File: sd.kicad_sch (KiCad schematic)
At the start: 10 parts, among them J5 Micro_SD_Card_Det1

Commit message: assigned footprint and created PCB file
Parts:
- C28: footprint (none) -> Capacitor_SMD:C_0805_2012Metric
- C29: footprint (none) -> Capacitor_SMD:C_0603_1608Metric
- J5: footprint (none) -> Connector_Card:microSD_HC_Hirose_DM3AT-SF-PEJM5
- R12, R13, R14, R15, R16, R17, R18: footprint (none) -> Resistor_SMD:R_0603_1608Metric
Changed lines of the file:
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@@
 			)
 		)
-		(property "Footprint" ""
+		(property "Footprint" "Resistor_SMD:R_0603_1608Metric"
 			(at 137.922 77.47 90)
 			(hide yes)
@@
 			)
 		)
-		(property "Footprint" ""
+		(property "Footprint" "Connector_Card:microSD_HC_Hirose_DM3AT-SF-PEJM5"
 			(at 64.77 114.3 0)
 			(hide yes)
@@
 			)
 		)
-		(property "Footprint" ""
+		(property "Footprint" "Resistor_SMD:R_0603_1608Metric"
 			(at 150.622 113.03 90)
 			(hide yes)
@@
 			)
 		)
-		(property "Footprint" ""
+		(property "Footprint" "Resistor_SMD:R_0603_1608Metric"
 			(at 173.482 113.03 90)
 			(hide yes)
@@
 			)
 		)
-		(property "Footprint" ""
+		(property "Footprint" "Resistor_SMD:R_0603_1608Metric"
 			(at 148.59 98.298 90)
 			(hide yes)
@@
 			)
 		)
-		(property "Footprint" ""
+		(property "Footprint" "Capacitor_SMD:C_0603_1608Metric"
 			(at 181.3052 100.33 0)
 			(hide yes)
@@
 			)
 		)
-		(property "Footprint" ""
+		(property "Footprint" "Resistor_SMD:R_0603_1608Metric"
 			(at 165.862 77.47 90)
 			(hide yes)
@@
 			)
 		)
-		(property "Footprint" ""
+		(property "Footprint" "Resistor_SMD:R_0603_1608Metric"
 			(at 154.432 77.47 90)
 			(hide yes)
@@
 			)
 		)
-		(property "Footprint" ""
+		(property "Footprint" "Resistor_SMD:R_0603_1608Metric"
 			(at 162.052 113.03 90)
 			(hide yes)
@@
 			)
 		)
-		(property "Footprint" ""
+		(property "Footprint" "Capacitor_SMD:C_0805_2012Metric"
 			(at 169.8752 100.33 0)
 			(hide yes)

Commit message: Updated with new power rails, added sensors and gps symbol
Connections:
- net +3.3V renamed +3.3V_HP
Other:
- note added: "PCB: For high speed layout, keep data lines, CMD and CLK length matched"
- note removed: "PCB: For high speed layout, keep data lines, CMD and CK length matched"
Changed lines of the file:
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@@
 		)
 	)
-	(text "PCB: For high speed layout, keep data lines, CMD and CK length matched"
+	(text "PCB: For high speed layout, keep data lines, CMD and CLK length matched"
 		(exclude_from_sim no)
-		(at 120.65 131.572 0)
+		(at 120.904 131.572 0)
 		(effects
 			(font
@@
 			)
 		)
-		(property "Value" "+3.3V"
+		(property "Value" "+3.3V_HP"
 			(at 194.31 100.3299 90)
 			(show_name no)
@@
 		(in_pos_files yes)
 		(dnp no)
-		(fields_autoplaced yes)
 		(property "Reference" "#PWR063"
 			(at 147.32 119.38 0)
@@
 			)
 		)
-		(property "Value" "+3.3V"
-			(at 139.7 119.3799 90)
-			(show_name no)
-			(do_not_autoplace no)
-			(effects
-				(font
-					(size 1.27 1.27)
-				)
-				(justify left)
+		(property "Value" "+3.3V_HP"
+			(at 135.382 119.38 90)
+			(show_name no)
+			(do_not_autoplace no)
+			(effects
+				(font
+					(size 1.27 1.27)
+				)
 			)
 		)
@@
 		(in_pos_files yes)
 		(dnp no)
-		(fields_autoplaced yes)
 		(property "Reference" "#PWR062"
 			(at 139.7 73.66 0)
@@
 			)
 		)
-		(property "Value" "+3.3V"
-			(at 139.7 64.77 0)
-			(show_name no)
-			(do_not_autoplace no)
-			(effects
-				(font
-					(size 1.27 1.27)
-				)
-			)
-		)
+		(property "Value" "+3.3V_HP"
+			(at 135.382 65.532 0)
+			(show_name no)
+			(do_not_autoplace no)
+			(effects
+				(font
+					(size 1.27 1.27)
+				)
+				(justify left)
+			)
+		)

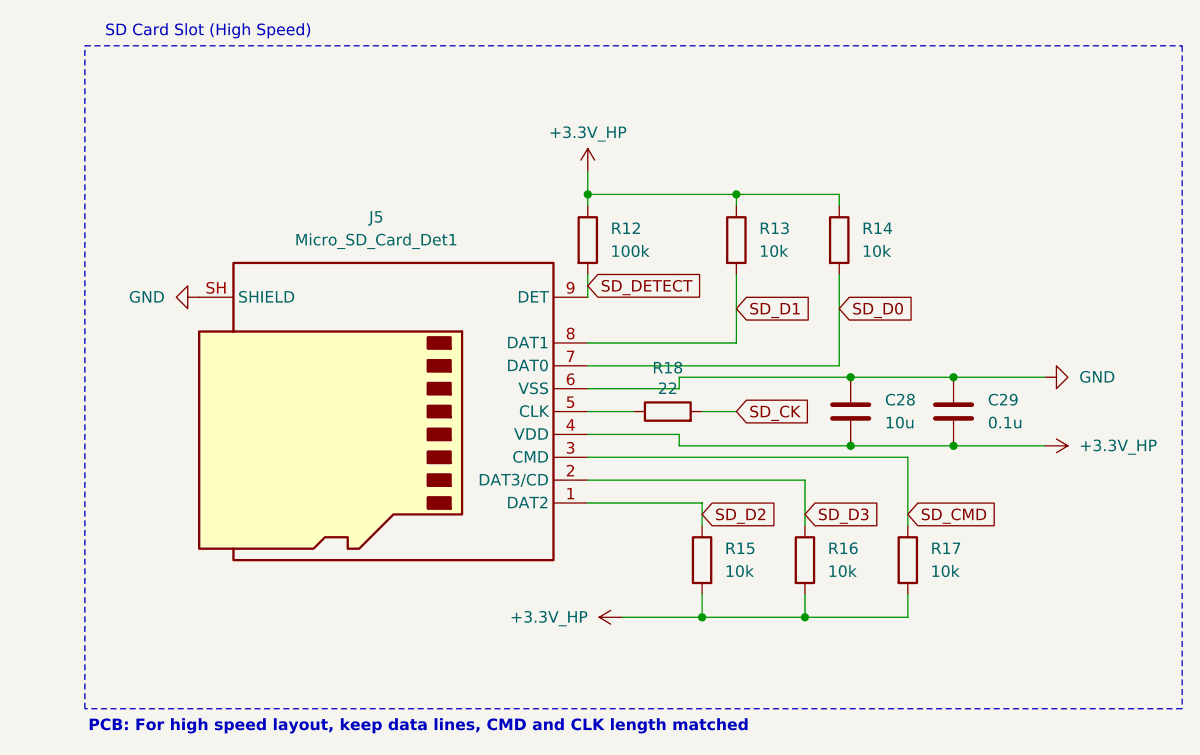
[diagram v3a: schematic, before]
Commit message: Updated with new power rails, added sensors and gps symbol
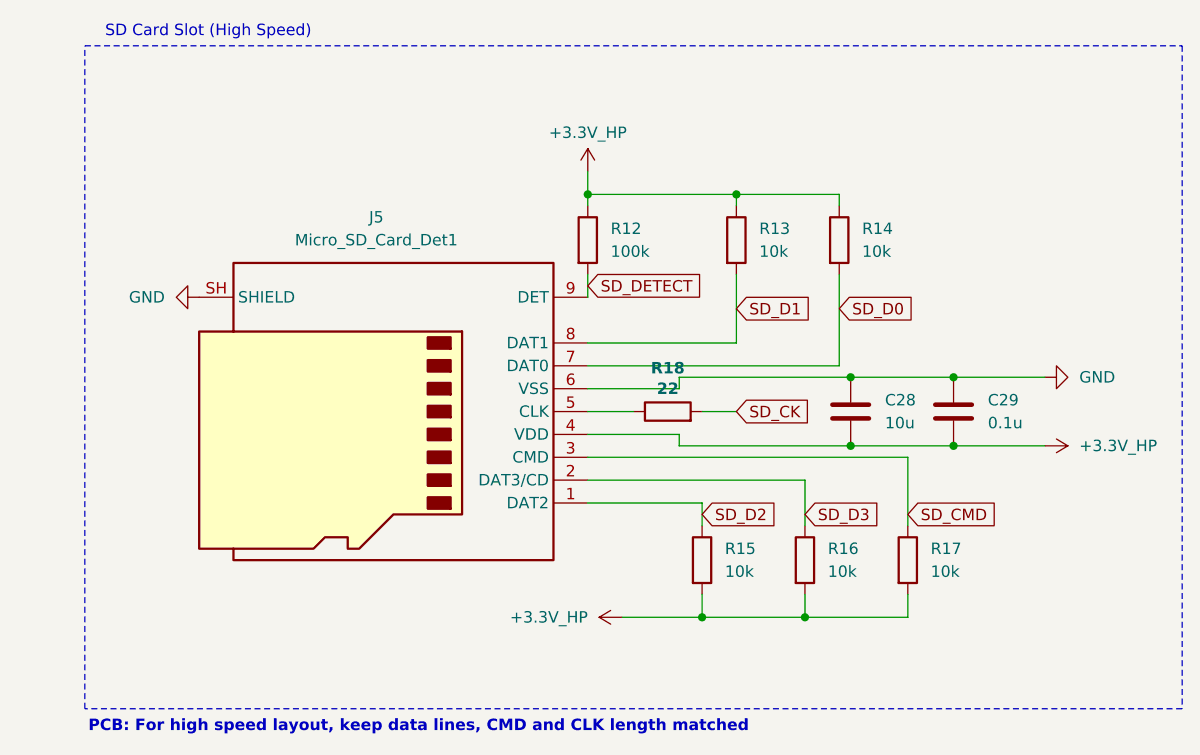
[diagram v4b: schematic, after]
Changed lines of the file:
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@@
 				(font
 					(size 1.27 1.27)
+					(thickness 0.254)
+					(bold yes)
 					(color 255 0 228 1)
 				)
@@
 				(font
 					(size 1.27 1.27)
+					(thickness 0.254)
+					(bold yes)
 					(color 255 0 255 1)
 				)

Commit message: added mux for usb, cleaned up schematic for pcb design, setup new pcb with correct size
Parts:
- C29: value 0.1u -> 100n
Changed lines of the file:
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@@
 			)
 		)
-		(property "Value" "0.1u"
+		(property "Value" "100n"
 			(at 184.15 97.7899 0)
 			(show_name no)
